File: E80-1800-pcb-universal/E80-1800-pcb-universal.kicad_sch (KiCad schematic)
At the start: 48 parts, among them J1 SPI, J2 BATT, J3 OLED, J4 USB_C_Receptacle_USB2.0, Q1 Q_NMOS_GSD, SW1 RST, SW2 BOOT, U1 SRV05-4, U2 XC6206P332MR, U3 STM32F072RBTx

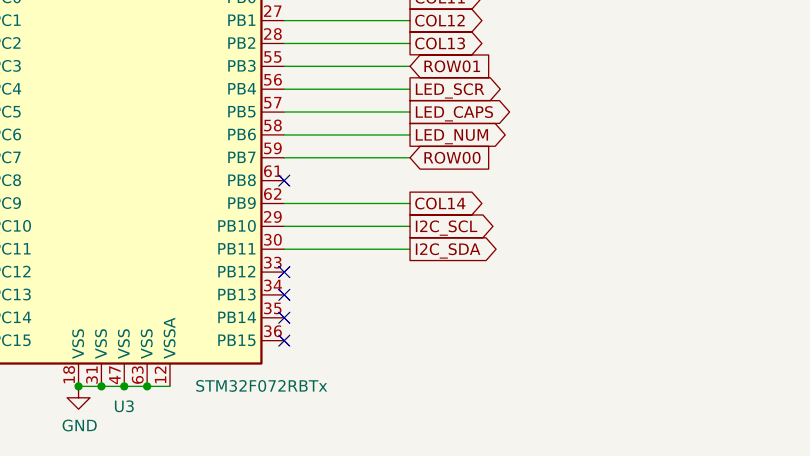
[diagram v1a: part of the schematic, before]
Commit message: add 2u 0 on numpad and rotary encoder
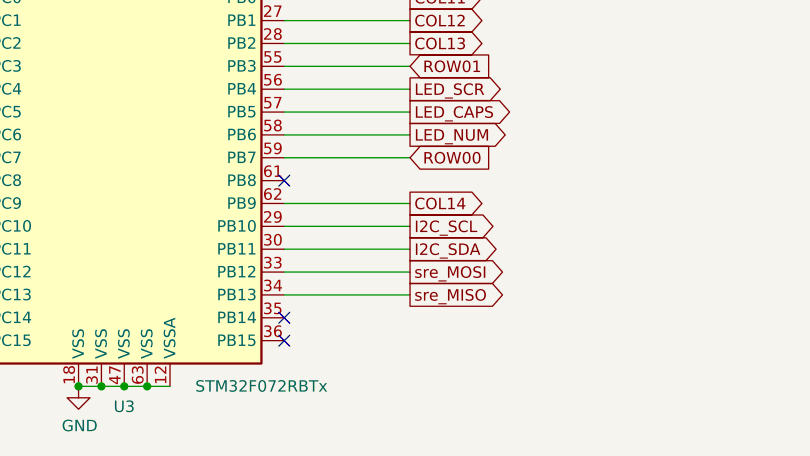
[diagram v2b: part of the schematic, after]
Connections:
- net sre_MOSI: now reaches U3.33 (PB12)
- net sre_MISO: now reaches U3.34 (PB13)
- no-connect marks 11 -> 9
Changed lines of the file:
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@@
   (junction (at 25.4 138.43) (diameter 0) (color 0 0 0 0)
   )
-  (no_connect (at 106.68 181.61))
   (no_connect (at 106.68 186.69))
   (no_connect (at 106.68 130.81))
@@
   (no_connect (at 106.68 168.91))
   (no_connect (at 41.91 53.34))
-  (no_connect (at 106.68 179.07))
   (no_connect (at 41.91 55.88))
   (no_connect (at 71.12 166.37))
@@
     (stroke (width 0) (type default) (color 0 0 0 0))
   )
+  (wire (pts (xy 106.68 179.07) (xy 120.65 179.07))
+    (stroke (width 0) (type default) (color 0 0 0 0))
+  )
   (wire (pts (xy 223.52 68.58) (xy 233.68 68.58))
     (stroke (width 0) (type default) (color 0 0 0 0))
@@
     (stroke (width 0) (type default) (color 0 0 0 0))
   )
+  (wire (pts (xy 106.68 181.61) (xy 120.65 181.61))
+    (stroke (width 0) (type default) (color 0 0 0 0))
+  )
   (polyline (pts (xy 199.39 16.51) (xy 199.39 45.72))
     (stroke (width 0) (type solid) (color 0 0 0 0))
@@
     )
   )
+  (global_label "sre_MISO" (shape output) (at 120.65 181.61 0) (fields_autoplaced)
+    (effects (font (size 1.27 1.27)) (justify left))
+    (property "Intersheet References" "${INTERSHEET_REFS}" (id 0) (at 131.4409 181.6894 0)
+      (effects (font (size 1.27 1.27)) (justify left) hide)
+    )
+  )
   (global_label "COL05" (shape output) (at 64.77 135.89 180) (fields_autoplaced)
     (effects (font (size 1.27 1.27)) (justify right))
@@
     )
   )
+  (global_label "sre_MOSI" (shape output) (at 120.65 179.07 0) (fields_autoplaced)
+    (effects (font (size 1.27 1.27)) (justify left))
+    (property "Intersheet References" "${INTERSHEET_REFS}" (id 0) (at 131.4409 179.1494 0)
+      (effects (font (size 1.27 1.27)) (justify left) hide)
+    )
+  )
   (global_label "COL17" (shape output) (at 64.77 171.45 180) (fields_autoplaced)
     (effects (font (size 1.27 1.27)) (justify right))
@@
       (reference "#PWR028") (unit 1) (value "+5V") (footprint "")
     )
+    (path "/00000000-0000-0000-0000-00005ecf9838/2688b646-f587-4bae-a899-b4f5b43b5058"
+      (reference "#PWR0101") (unit 1) (value "GND") (footprint "")
+    )
     (path "/00000000-0000-0000-0000-00005e74efe9"
       (reference "C1") (unit 1) (value "4.7uF") (footprint "Capacitor_SMD:C_0603_1608Metric")
@@
       (reference "D175") (unit 1) (value "3mm") (footprint "marbastlib-mx:LED_MX_3mm")
     )
+    (path "/00000000-0000-0000-0000-00005ecf9838/f84a5507-8f33-4bc4-9eba-8071380ce064"
+      (reference "D176") (unit 1) (value "3mm") (footprint "marbastlib-mx:LED_MX_3mm")
+    )
     (path "/00000000-0000-0000-0000-00005ef2a974"
       (reference "F1") (unit 1) (value "1206L050") (footprint "Fuse:Fuse_1206_3216Metric")
@@
       (reference "MX115") (unit 1) (value "MX_SW_solder") (footprint "marbastlib-mx:SW_MX_1u")
     )
+    (path "/00000000-0000-0000-0000-00005ecf9838/a67c7461-8057-4a50-8843-e35b8c7e3efe"
+      (reference "MX116") (unit 1) (value "MX_SW_solder") (footprint "marbastlib-mx:SW_MX_1u")
+    )
     (path "/00000000-0000-0000-0000-00005e71adb0"
       (reference "Q1") (unit 1) (value "Q_NMOS_GSD") (footprint "Package_TO_SOT_SMD:SOT-23")
@@
       (reference "S8") (unit 1) (value "np_+") (footprint "marbastlib-mx:STAB_MX_2u")
     )
+    (path "/00000000-0000-0000-0000-00005ecf9838/0d8c0908-41d6-4e5e-9492-41a142ecf84f"
+      (reference "S9") (unit 1) (value "np_0_2u") (footprint "marbastlib-mx:STAB_MX_2u")
+    )
     (path "/00000000-0000-0000-0000-00005e6313b3"
       (reference "SW1") (unit 1) (value "RST") (footprint "Button_Switch_SMD:SW_SPST_SKQG_WithoutStem")
@@
       (reference "SW5") (unit 1) (value "MX_SW_solder") (footprint "marbastlib-mx:SW_MX_1u")
     )
+    (path "/00000000-0000-0000-0000-00005ecf9838/c8def15a-750c-461f-b6cb-b317c3ce8a69"
+      (reference "SW6") (unit 1) (value "RotaryEncoder_Switch") (footprint "Rotary_Encoder:RotaryEncoder_Alps_EC11E-Switch_Vertical_H20mm")
+    )
     (path "/00000000-0000-0000-0000-00005ef1b07d"

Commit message: prepare for jlcpcb
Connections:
- net ENCB: now reaches U3.35 (PB14)
- net ENCA: now reaches U3.36 (PB15)
- no-connect marks 9 -> 7
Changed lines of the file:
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@@
   (junction (at 25.4 138.43) (diameter 0) (color 0 0 0 0)
   )
-  (no_connect (at 106.68 186.69))
   (no_connect (at 106.68 130.81))
   (no_connect (at 106.68 140.97))
@@
   (no_connect (at 41.91 55.88))
   (no_connect (at 71.12 166.37))
-  (no_connect (at 106.68 184.15))
   (wire (pts (xy 233.68 60.96) (xy 243.84 60.96))
     (stroke (width 0) (type default) (color 0 0 0 0))
@@
     )
   )
+  (global_label "ENCA" (shape input) (at 106.68 186.69 0) (fields_autoplaced)
+    (effects (font (size 1.27 1.27)) (justify left))
+    (property "Intersheet References" "${INTERSHEET_REFS}" (id 0) (at 113.8423 186.6106 0)
+      (effects (font (size 1.27 1.27)) (justify left) hide)
+    )
+  )
   (global_label "SPI_IRQ" (shape input) (at 120.65 113.03 0) (fields_autoplaced)
     (effects (font (size 1.27 1.27)) (justify left))
@@
     )
   )
+  (global_label "ENCB" (shape input) (at 106.68 184.15 0) (fields_autoplaced)
+    (effects (font (size 1.27 1.27)) (justify left))
+    (property "Intersheet References" "${INTERSHEET_REFS}" (id 0) (at 114.0237 184.0706 0)
+      (effects (font (size 1.27 1.27)) (justify left) hide)
+    )
+  )
